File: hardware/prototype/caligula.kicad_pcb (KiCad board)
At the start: 2 copper layers, 70.3 x 67.5 mm, 86 parts, among them J1 USB2UART, J2 1.47 IPS LCD, J3 ConnBattery, J4 RTD_PT100, Q1 SS8050, Q2 SS8050, Q3 SS8050, Q5 SS8050, SW1 RST, SW2 IN1, SW3 Boot, SW4 IN2, SW5 IN4, SW6 IN4, SW7 IN5, U1 CH340C, U2 ESP32-S3-WROOM-1, U3 TPS63001_SEPIC_3V3, U4 MAX31865xTP, U5 BQ24075RGT_DPPM, U7 BQ27421YZFR-G1A

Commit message: feat: update simulation to use +- 3.6v
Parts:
- removed C18, C19, C20, C24, C9: 100nF, Capacitor_SMD:C_0805_2012Metric_Pad1.18x1.45mm_HandSolder
- removed C21: 0.47uF, Capacitor_SMD:C_0805_2012Metric_Pad1.18x1.45mm_HandSolder
- removed the D1 at (123.2, 75.4)
- removed JP2: 2_Wire, Jumper:SolderJumper-2_P1.3mm_Open_TrianglePad1.0x1.5mm
- removed Q5: SS8050, Package_TO_SOT_SMD:SOT-23_Handsoldering
- removed the R8 at (123.5, 73.1)
- removed SW7: IN5, Button_Switch_SMD:SW_SPST_Omron_B3FS-100xP
- removed U7: BQ27421YZFR-G1A, easyeda2kicad:DSBGA-9_L1.5-W1.5-R3-C3-P0.50-BL
- added C25: 100nF, Capacitor_SMD:C_0805_2012Metric_Pad1.18x1.45mm_HandSolder, F.Cu at (-88.0, -0.02)
- added C26: 10uF / >5V, Capacitor_SMD:C_0805_2012Metric_Pad1.18x1.45mm_HandSolder, F.Cu at (-88.0, 2.99)
- added C27: 10uF / >10V, Capacitor_SMD:C_0805_2012Metric_Pad1.18x1.45mm_HandSolder, F.Cu at (-88.0, 6.00)
- added C28: 2n2F, Capacitor_SMD:C_0805_2012Metric_Pad1.18x1.45mm_HandSolder, F.Cu at (32.0, -170.0)
- added C29: 100nF, Capacitor_SMD:C_0805_2012Metric_Pad1.18x1.45mm_HandSolder, F.Cu at (165.2, -172.3)
- added C30: 10uF, Capacitor_SMD:C_0805_2012Metric_Pad1.18x1.45mm_HandSolder, F.Cu at (-41.3, 120.3)
- added C31: 0.1uF, Capacitor_SMD:C_0805_2012Metric_Pad1.18x1.45mm_HandSolder, F.Cu at (-41.3, 123.3)
- added C32: 10uF, Capacitor_SMD:C_0805_2012Metric_Pad1.18x1.45mm_HandSolder, F.Cu at (-41.3, 126.4)
- added C33: 10uF, Capacitor_SMD:C_0805_2012Metric_Pad1.18x1.45mm_HandSolder, F.Cu at (-41.3, 129.4)
- added Card1: TF PUSH, easyeda2kicad:TF-SMD_TF-PUSH, F.Cu at (340.9, 17.3)
- added J5: lcd jumper, Connector_PinHeader_2.54mm:PinHeader_1x08_P2.54mm_Vertical, B.Cu at (106.6, -174.2)
- added J6: lcd jumper, Connector_PinHeader_2.54mm:PinHeader_1x08_P2.54mm_Vertical, B.Cu at (102.0, -174.2)
- added J7: lcd jumper, Connector_PinHeader_2.54mm:PinHeader_1x08_P2.54mm_Vertical, B.Cu at (97.4, -174.2)
- added J8: PH Sensor, Connector_Coaxial:BNC_Amphenol_B6252HB-NPP3G-50_Horizontal, B.Cu at (19.7, -154.4)
- added L2: 22uH 1A, Inductor_SMD:L_Bourns_SRP7028A_7.3x6.6mm, F.Cu at (-49.7, 126.0)
- added R29: 4M7, Resistor_SMD:R_0805_2012Metric_Pad1.20x1.40mm_HandSolder, F.Cu at (35.2, -156.0)
- added R30: 10K, Resistor_SMD:R_0805_2012Metric_Pad1.20x1.40mm_HandSolder, F.Cu at (35.2, -153.1)
- added R31: 1K, Resistor_SMD:R_0805_2012Metric_Pad1.20x1.40mm_HandSolder, F.Cu at (40.0, -164.8)
- added R32: 9K, Resistor_SMD:R_0805_2012Metric_Pad1.20x1.40mm_HandSolder, F.Cu at (40.0, -161.9)
- added R33: 20K, Resistor_SMD:R_0805_2012Metric_Pad1.20x1.40mm_HandSolder, F.Cu at (40.0, -158.9)
- added R34: 25K, Resistor_SMD:R_0805_2012Metric_Pad1.20x1.40mm_HandSolder, F.Cu at (40.0, -156.0)
- added R35: 5K1, Resistor_SMD:R_0805_2012Metric_Pad1.20x1.40mm_HandSolder, F.Cu at (327.8, -58.7)
- added R36: 100, Resistor_SMD:R_0805_2012Metric_Pad1.20x1.40mm_HandSolder, F.Cu at (-35.0, 124.0)
- added R37: 5K1, Resistor_SMD:R_0805_2012Metric_Pad1.20x1.40mm_HandSolder, F.Cu at (332.5, -67.5)
- added R38: 22 / 33, Resistor_SMD:R_0805_2012Metric_Pad1.20x1.40mm_HandSolder, F.Cu at (332.5, -64.6)
- added R39: 22 / 33, Resistor_SMD:R_0805_2012Metric_Pad1.20x1.40mm_HandSolder, F.Cu at (332.5, -61.6)
- added U10: TL431LP, Package_TO_SOT_THT:TO-92_Inline, B.Cu at (23.2, -147.9)
- added U11: TPS63002, Package_SON:Texas_DRC0010J_ThermalVias, F.Cu at (-35.2, 129.5)
- added U6: ADS1115IDGS, Package_SO:TSSOP-10_3x3mm_P0.5mm, F.Cu at (162.7, -166.4)
- added U8: OPA2197xD, Package_SO:SOIC-8_3.9x4.9mm_P1.27mm, F.Cu at (32.5, -163.6)
- J3: footprint Connector_PinHeader_2.54mm:PinHeader_1x03_P2.54mm_Vertical -> Connector_JST:JST_XH_S3B-XH-A_1x03_P2.50mm_Horizontal
- J4: value RTD_PT100 -> USB2UART; footprint TerminalBlock_Phoenix:TerminalBlock_Phoenix_PT-1,5-3-5.0-H_1x03_P5.00mm_Horizontal -> Connector_USB:USB_C_Receptacle_GCT_USB4110; moved to F.Cu
- JP1: value 3_OR_2_Wire -> TS_unused; footprint Jumper:SolderJumper-3_P1.3mm_Open_RoundedPad1.0x1.5mm -> Jumper:SolderJumper-2_P1.3mm_Open_RoundedPad1.0x1.5mm
- R10: value 1k -> 51k; moved to F.Cu
- R19: value 430 1% -> 4k7
- R22: value 4K7 -> 4k7
- R23: value 4K7 -> 10K
- R26: value 10K -> 51k
- R27: value 1k -> 51k
- R28: value 10k -> 51k
- SW1, SW3: footprint Button_Switch_SMD:SW_SPST_PTS810 -> Button_Switch_SMD:SW_SPST_EVQP7A
- SW2, SW4, SW5, SW6: footprint Button_Switch_SMD:SW_SPST_Omron_B3FS-100xP -> keyswitches.pretty-master:Kailh_socket_MX_reversible_platemount
- U4: value MAX31865xTP -> ICL7660; footprint Package_DFN_QFN:TQFN-20-1EP_5x5mm_P0.65mm_EP3.25x3.25mm -> Package_SO:SOIC-8_3.9x4.9mm_P1.27mm
- moved C1 314.4 mm to (305.6, -166.8)
- moved C3 314.4 mm to (320.0, -157.0)
- moved C5 314.4 mm to (305.6, -145.2)
- moved C6 314.4 mm to (275.2, -156.8)
- moved R1 314.4 mm to (305.6, -164.8)
- moved R3 314.4 mm to (320.0, -155.0)
- moved R7 314.4 mm to (305.6, -143.1)
- moved R9 314.4 mm to (275.2, -154.7)
- moved SW2 314.4 mm to (297.5, -160.7)
- moved SW4 314.4 mm to (312.3, -150.1)
- moved SW5 314.4 mm to (297.7, -140.2)
- moved SW6 314.4 mm to (283.4, -150.0)
- moved U1 286.4 mm to (205.7, -157.4)
- moved C7 286.4 mm to (198.9, -156.9)
- moved J1 286.4 mm to (206.2, -143.3)
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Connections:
- JP1 pad 1: Net-(J4-Pin_3) -> Net-(JP1-A)
- JP1 pad 2: Net-(JP1-C) -> /TS
- R10 pad 2: /IN5 -> /MOSI2
- R19 pad 1: Net-(U4-BIAS) -> +3.3V
- R19 pad 2: Net-(U4-ISENSOR) -> /I2C_SCL
- R23 pad 1: +3.3V -> Net-(JP1-A)
- R23 pad 2: /I2C_SCL -> GND
- R26 pad 1: /GPOUT -> +3.3V
- R26 pad 2: GND -> /MISO2
- R27 pad 2: Net-(Q5-C) -> /MMC_INT
- R28 pad 2: Net-(Q5-B) -> /MMC_CS
- U2 pad 10: /IN1 -> unconnected-(U2-IO17-Pad10)
- U2 pad 11: /IN2 -> /ADS1115_DRDY
- U2 pad 12: /MAX31865DRDY -> /MMC_INT
- U2 pad 13: /IN3 -> /USB_DM
- U2 pad 14: /IN4 -> /USB_DP
- U2 pad 16: unconnected-(U2-IO46-Pad16) -> /IN5
- U2 pad 17: /MAX31865CS -> /MMC_CS
- U2 pad 23: /IN5 -> unconnected-(U2-IO21-Pad23)
- U2 pad 26: unconnected-(U2-IO45-Pad26) -> /IN4
- U2 pad 33: unconnected-(U2-IO40-Pad33) -> /IN1
- U2 pad 34: unconnected-(U2-IO41-Pad34) -> /IN2
- U2 pad 35: unconnected-(U2-IO42-Pad35) -> /IN3
- U4 pad 1: Net-(U4-BIAS) -> unconnected-(U4-NC-Pad1)
- U4 pad 2: Net-(U4-BIAS) -> Net-(U4-CAP+)
- U4 pad 3: Net-(U4-ISENSOR) -> GND
- U4 pad 4: Net-(U4-ISENSOR) -> Net-(U4-CAP-)
- U4 pad 5: Net-(J4-Pin_3) -> -5V
- U4 pad 6: Net-(JP1-C) -> unconnected-(U4-LV-Pad6)
- U4 pad 7: Net-(J4-Pin_2) -> unconnected-(U4-OSC-Pad7)
- U4 pad 8: Net-(J4-Pin_1) -> +5V
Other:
- outline, holes or cut-outs redrawn

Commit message: feat: update component placement
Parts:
- removed C30, C32, C33: 10uF, Capacitor_SMD:C_0805_2012Metric_Pad1.18x1.45mm_HandSolder
- removed C31: 0.1uF, Capacitor_SMD:C_0805_2012Metric_Pad1.18x1.45mm_HandSolder
- removed L2: 22uH 1A, Inductor_SMD:L_Bourns_SRP7028A_7.3x6.6mm
- removed R34: 25K, Resistor_SMD:R_0805_2012Metric_Pad1.20x1.40mm_HandSolder
- removed R36: 100, Resistor_SMD:R_0805_2012Metric_Pad1.20x1.40mm_HandSolder
- removed U10: TL431LP, Package_TO_SOT_THT:TO-92_Inline
- removed U11: TPS63002, Package_SON:Texas_DRC0010J_ThermalVias
- added C18: 100nF, Capacitor_SMD:C_0805_2012Metric_Pad1.18x1.45mm_HandSolder, F.Cu at (99.9, 67.1)
- added C19: 100nF, Capacitor_SMD:C_0805_2012Metric_Pad1.18x1.45mm_HandSolder, F.Cu at (99.9, 69.4)
- added C20: 100nF, Capacitor_SMD:C_0805_2012Metric_Pad1.18x1.45mm_HandSolder, F.Cu at (100.6, 81.7)
- added C9: 100nF, Capacitor_SMD:C_0805_2012Metric_Pad1.18x1.45mm_HandSolder, F.Cu at (52.0, 89.5)
- added J10: PT100_CONN, Connector_Audio:Jack_XLR_Neutrik_NC3FAH1_Horizontal, B.Cu at (82.8, 58.4)
- added JP2: 3_OR_2_Wire, Jumper:SolderJumper-3_P1.3mm_Open_RoundedPad1.0x1.5mm, F.Cu at (98.4, 84.2)
- added JP3: 2_Wire, Jumper:SolderJumper-2_P1.3mm_Open_TrianglePad1.0x1.5mm, F.Cu at (98.1, 87.5)
- added R40: 430 1%, Resistor_SMD:R_0805_2012Metric_Pad1.20x1.40mm_HandSolder, F.Cu at (93.9, 75.6)
- added SW7: MST22D18G2, easyeda2kicad:SW-SMD_MST22D18G2, F.Cu at (53.8, 141.2)
- added U7: MAX31865xTP, Package_DFN_QFN:TQFN-20-1EP_5x5mm_P0.65mm_EP3.25x3.25mm, F.Cu at (100.1, 75.6)
- Card1, R10, R26, R27, R28: moved to B.Cu
- R32: value 9K -> 4k5
- R33: value 20K -> 10K
- moved C1 334.3 mm to (101.3, 97.8)
- moved R1 334.3 mm to (101.3, 99.8)
- moved C6 331.0 mm to (62.1, 96.6)
- moved R9 331.0 mm to (62.1, 98.6)
- moved SW2 330.9 mm to (92.1, 98.8)
- moved SW5 329.0 mm to (92.2, 116.8)
- moved C5 326.5 mm to (102.8, 110.7)
- moved R7 326.5 mm to (102.8, 112.8)
- moved SW6 325.1 mm to (74.0, 98.8)
- moved C3 321.9 mm to (122.3, 97.1)
- moved R3 321.9 mm to (122.3, 99.1)
- moved SW4 319.0 mm to (112.8, 98.8)
- moved C29 293.4 mm to (53.1, 98.8), turned to 180 degrees
- moved U6 291.4 mm to (53.1, 103.6)
- moved R19 285.5 mm to (59.1, 101.1), turned to -90 degrees
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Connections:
- net -5V renamed -3V3
- C14 pad 1: Net-(U3-EN) -> Net-(U3-PS/SYNC)
- C25 pad 1: +5V -> +3.3V
- Card1 pad 3: /MOSI2 -> /MOSI
- Card1 pad 5: /SCK2 -> /SCK
- Card1 pad 7: /MISO2 -> /MISO
- R10 pad 2: /MOSI2 -> /MOSI
- R15 pad 2: Net-(U3-EN) -> Net-(U3-PS/SYNC)
- R26 pad 2: /MISO2 -> /MISO
- R30 pad 1: +2V5 -> +3.3V
- R33 pad 1: Net-(U8B-+) -> Net-(R32-Pad1)
- R33 pad 2: Net-(R32-Pad1) -> Net-(U8B-+)
- U2 pad 24: unconnected-(U2-IO47-Pad24) -> /MAX31865DRDY
- U2 pad 25: unconnected-(U2-IO48-Pad25) -> /MAX31865CS
- U3 pad 6: Net-(U3-EN) -> /TPS_EN
- U3 pad 7: Net-(U3-EN) -> Net-(U3-PS/SYNC)
- U3 pad 8: Net-(U3-EN) -> Net-(U3-PS/SYNC)
- U4 pad 6: unconnected-(U4-LV-Pad6) -> GND
- U4 pad 8: +5V -> +3.3V
- U8 pad 8: +5V -> +3.3V
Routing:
- removed copper zone on B.Cu, net (none)
- removed copper zone on F.Cu, net (none)
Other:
- board size 70.3 x 67.5 mm -> 90 x 108.5 mm

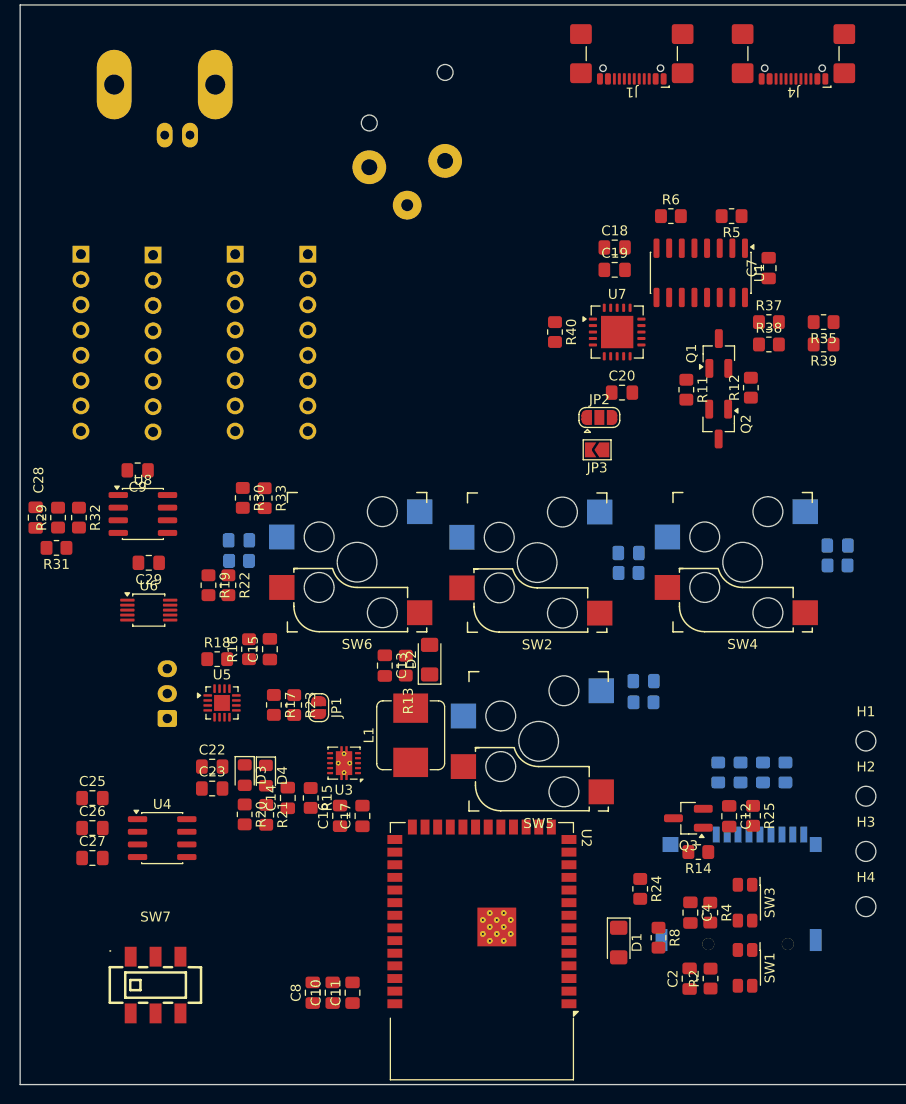
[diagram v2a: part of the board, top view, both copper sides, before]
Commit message: feat: start routing prototype
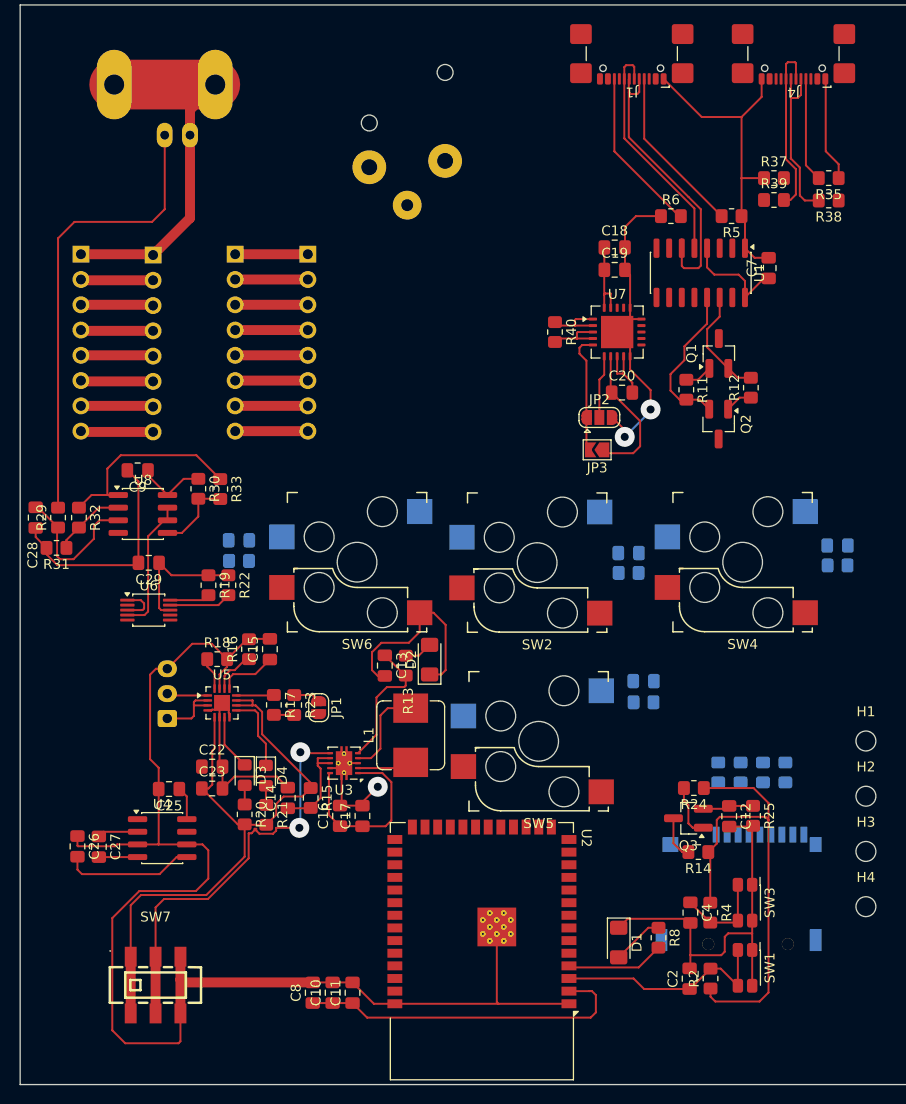
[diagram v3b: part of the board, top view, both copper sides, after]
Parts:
- moved R38 15.7 mm to (121.4, 62.4), turned to 180 degrees
- moved R39 15.4 mm to (115.9, 62.4), turned to 0 degrees
- moved R35 14.5 mm to (121.4, 60.1)
- moved R37 14.5 mm to (115.9, 60.1)
- moved R24 11.5 mm to (107.8, 121.5), turned to 180 degrees
- moved C25 7.75 mm to (55.1, 121.5), turned to 180 degrees
- moved R30 4.56 mm to (58.0, 91.4)
- moved R33 4.56 mm to (60.2, 91.4)
- moved C26 2.38 mm to (45.9, 127.3), turned to -90 degrees
- moved C27 1.30 mm to (48.0, 127.3), turned to -90 degrees
- turned C28 to -90 degrees
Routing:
- net GND: track 0.00 -> 371.8 mm, vias 0 -> 3
- net +3.3V: track 0.00 -> 150.6 mm
- net VDD: track 0.00 -> 78.7 mm
- net Net-(J8-In): track 0.00 -> 46.4 mm
- net /TPS_EN: track 0.00 -> 41.3 mm, vias 0 -> 2
- net Net-(U1-UD-): track 0.00 -> 29.1 mm
- net Net-(U1-UD+): track 0.00 -> 23.5 mm
- net /EN: track 0.00 -> 22.6 mm
- net Net-(R32-Pad1): track 0.00 -> 21.1 mm
- net Net-(J4-D+-PadA6): track 0.00 -> 17.6 mm
- net Net-(J1-CC1): track 0.00 -> 17.0 mm
- net Net-(J4-D--PadA7): track 0.00 -> 17.0 mm
- net Net-(J1-CC2): track 0.00 -> 16.7 mm
- net /DTR: track 0.00 -> 15.5 mm
- net Net-(U8A-+): track 0.00 -> 14.7 mm
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
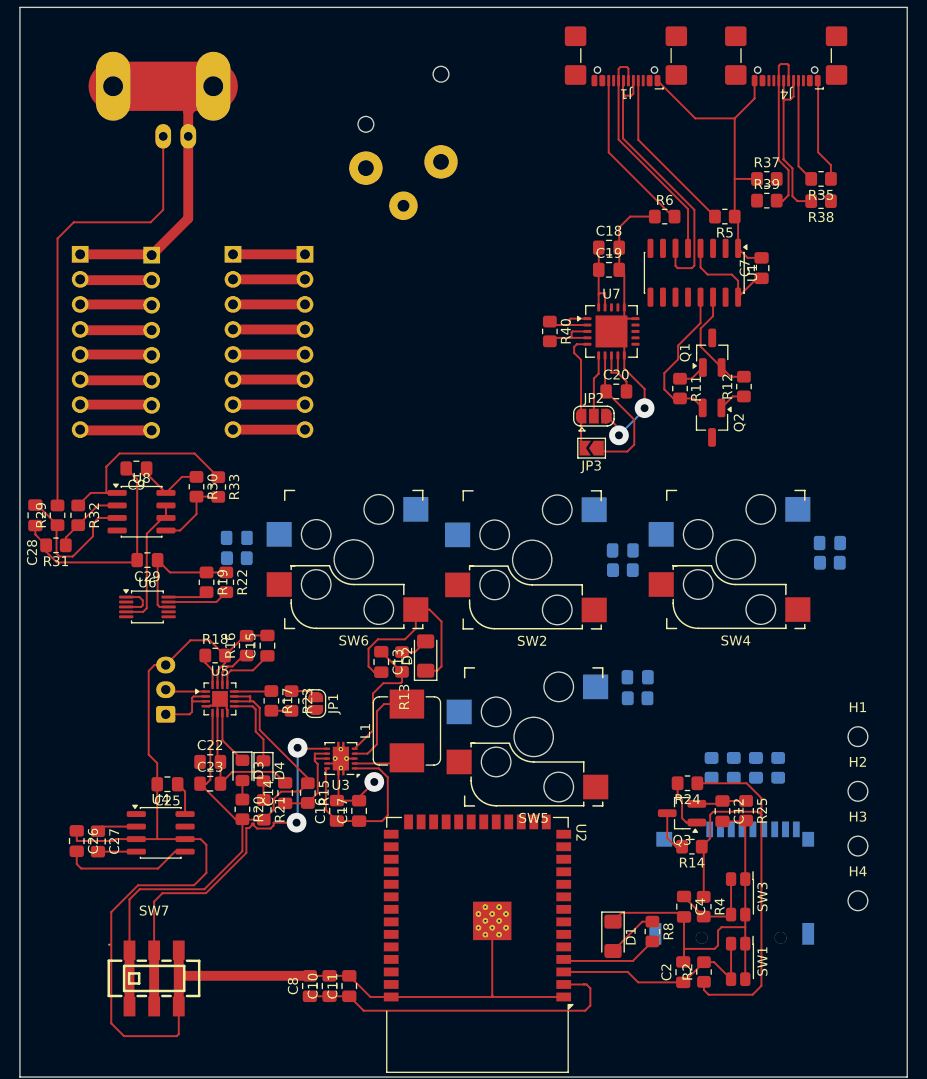
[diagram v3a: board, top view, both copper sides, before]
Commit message: feat: update routing phase 1
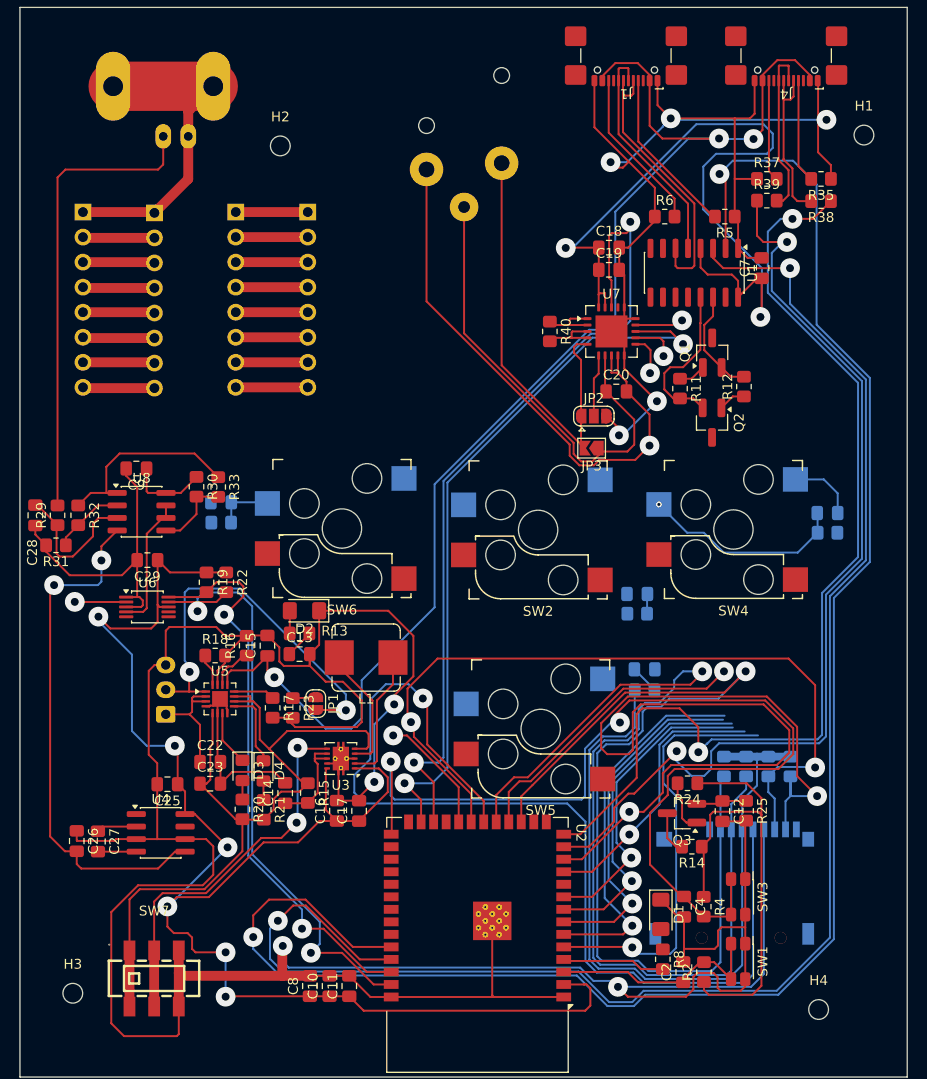
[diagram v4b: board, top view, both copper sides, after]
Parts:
- moved H2 87.9 mm to (66.5, 56.8)
- moved H3 81.0 mm to (45.5, 142.8)
- moved H1 61.0 mm to (125.8, 55.7)
- moved D2 13.1 mm to (69.0, 104.0), turned to 180 degrees
- moved H4 11.7 mm to (121.2, 144.4)
- moved R13 10.8 mm to (68.5, 106.2), turned to 180 degrees
- moved L1 8.52 mm to (75.2, 108.7), turned to 180 degrees
- moved C13 8.33 mm to (68.5, 108.3), turned to 0 degrees
- moved J10 6.15 mm to (89.0, 58.5)
- moved R28 5.50 mm to (111.5, 119.8)
- moved D1 5.34 mm to (105.2, 134.8)
- moved C1 4.65 mm to (102.8, 102.2), turned to 180 degrees
- moved R1 4.65 mm to (102.8, 104.2)
- moved J2 4.30 mm to (46.5, 63.5)
- moved J6 4.30 mm to (69.3, 63.5)
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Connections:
- U2 pad 16: /IN5 -> unconnected-(U2-IO46-Pad16)
- U2 pad 26: /IN4 -> unconnected-(U2-IO45-Pad26)
- U2 pad 32: /GPOUT -> /IN1
- U2 pad 33: /IN1 -> /IN2
- U2 pad 34: /IN2 -> /IN3
- U2 pad 35: /IN3 -> /IN4
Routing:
- net +3.3V: track 150.6 -> 375.7 mm, vias 0 -> 8
- net /RXD0: track 0.00 -> 183.7 mm, vias 0 -> 2
- net GND: track 371.8 -> 551.1 mm, vias 3 -> 9
- net /TXD0: track 0.00 -> 161.7 mm, vias 0 -> 2
- net VBUS: track 5.91 -> 132.5 mm, vias 0 -> 3
- net /SCK: track 7.28 -> 110.8 mm, vias 0 -> 1
- net /USB_DP: track 0.00 -> 103.4 mm, vias 0 -> 2
- net /MMC_CS: track 0.00 -> 103.3 mm, vias 0 -> 1
- net /MOSI: track 7.28 -> 108.4 mm, vias 0 -> 1
- net /USB_DM: track 0.00 -> 99.0 mm, vias 0 -> 2
- net /MMC_INT: track 0.00 -> 98.4 mm, vias 0 -> 2
- net /IO0: track 9.32 -> 101.4 mm, vias 0 -> 2
- net /MAX31865DRDY: track 0.00 -> 84.4 mm, vias 0 -> 2
- net /MISO: track 0.00 -> 79.1 mm, vias 0 -> 2
- net /MAX31865CS: track 0.00 -> 74.2 mm, vias 0 -> 2
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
